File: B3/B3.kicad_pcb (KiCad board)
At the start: 4 copper layers, 100 x 100 mm, 89 parts, among them SW301 SW_SPDT, U301 74HC00, U302 74HC125, U303 74HC74, U304 74HC74, U305 74HC74, U306 74HC32, U307 74HC299, U308 74HC193, U309 74HC00, U310 74HC244, U311 74HC377, U312 74HC244, U313 74HC299, U314 74HC32, U315 74HC193, U316 74HC00, U317 74HC74, U318 74HC08, U319 74HC32, U320 74HC00, U321 74HC00, U322 74HC00, U323 74HC00, U324 74HC00, U325 74HC08, U326 74HC08, U327 74HC377, U328 74HC00, U329 74HC00, U330 74HC74, U331 74HC74, U332 74HC74, U333 74HC74, U334 74HC74, U335 74HC04, U336 74HC244, U337 74HC08, U338 74HC32, U339 74HC08, U340 74HC74

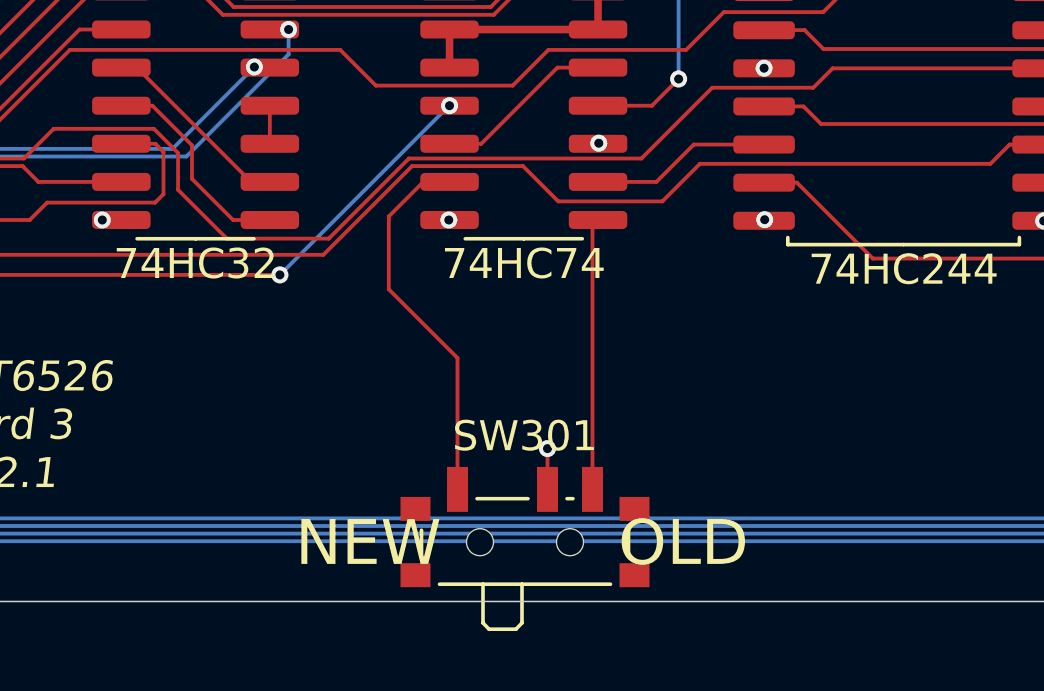
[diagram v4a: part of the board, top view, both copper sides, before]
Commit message: Issue #12 diagnosis
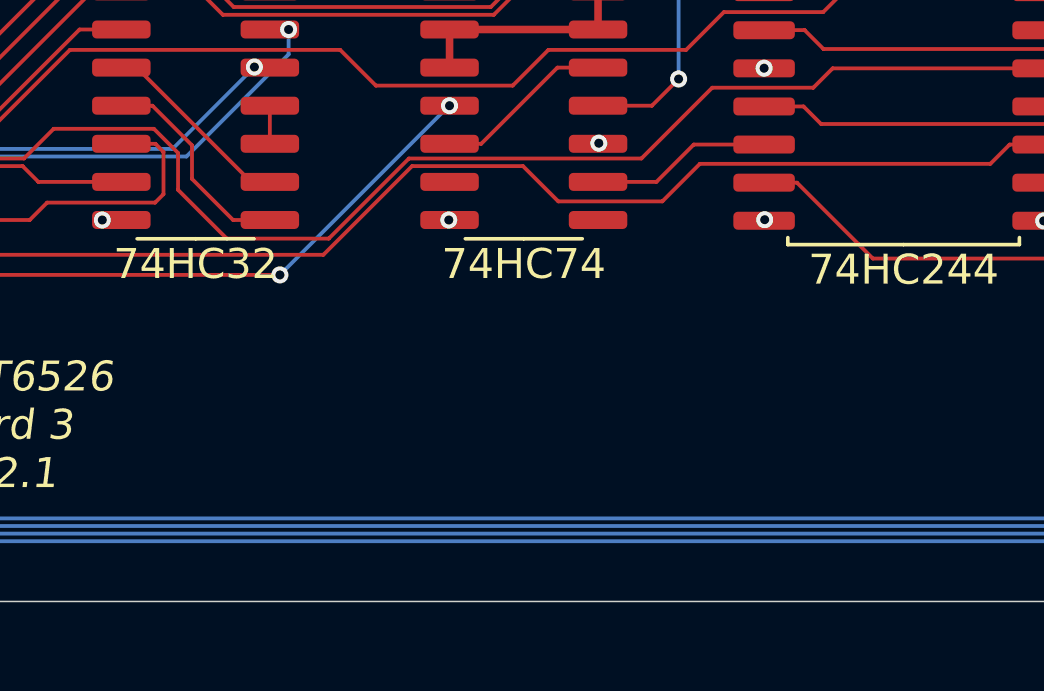
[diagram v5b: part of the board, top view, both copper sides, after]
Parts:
- removed SW301: SW_SPDT, Button_Switch_SMD:SW_SPDT_PCM12
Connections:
- U334 pad 6: Net-(U334-Pad6) -> unconnected-(U334-Pad6)
- U334 pad 8: Net-(U334-Pad8) -> ~{IRQ}
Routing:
- net ~{IRQ}: track 55.2 -> 0.00 mm, vias 1 -> 0
- net Net-(U334-Pad6): track 11.7 -> 0.00 mm
- net Net-(U334-Pad8): track 8.80 -> 0.00 mm
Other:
- board text removed: "NEW OLD"
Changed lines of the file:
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@@
   (net 155 "/icr/icrControl/ICR1")
   (net 156 "Net-(U334-Pad4)")
-  (net 157 "Net-(U334-Pad6)")
+  (net 157 "unconnected-(U334-Pad6)")
   (net 158 "/icr/icrControl/ICR7")
   (net 159 "Net-(U337-Pad8)")
@@
   (net 212 "unconnected-(U340-Pad8)")
   (net 213 "unconnected-(U340-Pad9)")
-  (net 214 "Net-(U334-Pad8)")
   (footprint "Package_SO:SO-14_3.9x8.65mm_P1.27mm" (layer "F.Cu")
     (at 111.95 128.48)
@@
     )
   )
-  (footprint "Button_Switch_SMD:SW_SPDT_PCM12" (layer "F.Cu")
-    (at 166.69 142.7)
-    (descr "Ultraminiature Surface Mount Slide Switch, right-angle, https://www.ckswitches.com/media/1424/pcm.pdf")
-    (property "Sheetfile" "icrControl.kicad_sch")
-    (property "Sheetname" "icrControl")
-    (attr smd)
-    (fp_text reference "SW301" (at 0 -3.2) (layer "F.SilkS")
-      (effects (font (size 1 1) (thickness 0.15)))
-    )
-    (fp_text value "SW_SPDT" (at 0 4.25) (layer "F.Fab")
-      (effects (font (size 1 1) (thickness 0.15)))
-    )
-    (fp_text user "${REFERENCE}" (at 0 -3.2) (layer "F.Fab")
-      (effects (font (size 1 1) (thickness 0.15)))
-    )
-    (fp_line (start 3.45 0.72) (end 3.45 -0.07) (layer "F.SilkS") (width 0.12))
-    (fp_line (start -0.1 3.02) (end -0.1 1.73) (layer "F.SilkS") (width 0.12))
-    (fp_line (start -1.2 3.23) (end -0.3 3.23) (layer "F.SilkS") (width 0.12))
-    (fp_line (start 1.4 -1.12) (end 1.6 -1.12) (layer "F.SilkS") (width 0.12))
-    (fp_line (start -0.1 3.02) (end -0.3 3.23) (layer "F.SilkS") (width 0.12))
-    (fp_line (start -1.4 3.02) (end -1.2 3.23) (layer "F.SilkS") (width 0.12))
-    (fp_line (start -3.45 -0.07) (end -3.45 0.72) (layer "F.SilkS") (width 0.12))
-    (fp_line (start -2.85 1.73) (end 2.85 1.73) (layer "F.SilkS") (width 0.12))
-    (fp_line (start -1.4 1.73) (end -1.4 3.02) (layer "F.SilkS") (width 0.12))
-    (fp_line (start -1.6 -1.12) (end 0.1 -1.12) (layer "F.SilkS") (width 0.12))
-    (fp_line (start -4.4 -2.45) (end 4.4 -2.45) (layer "F.CrtYd") (width 0.05))
-    (fp_line (start -1.65 3.4) (end -1.65 2.1) (layer "F.CrtYd") (width 0.05))
-    (fp_line (start 4.4 2.1) (end 1.65 2.1) (layer "F.CrtYd") (width 0.05))
-    (fp_line (start -1.65 2.1) (end -4.4 2.1) (layer "F.CrtYd") (width 0.05))
-    (fp_line (start 4.4 -2.45) (end 4.4 2.1) (layer "F.CrtYd") (width 0.05))
-    (fp_line (start -4.4 2.1) (end -4.4 -2.45) (layer "F.CrtYd") (width 0.05))
-    (fp_line (start 1.65 2.1) (end 1.65 3.4) (layer "F.CrtYd") (width 0.05))
-    (fp_line (start 1.65 3.4) (end -1.65 3.4) (layer "F.CrtYd") (width 0.05))
-    (fp_line (start -3.35 -1) (end -3.35 1.6) (layer "F.Fab") (width 0.1))
-    (fp_line (start -3.35 1.6) (end 3.35 1.6) (layer "F.Fab") (width 0.1))
-    (fp_line (start -1.4 1.65) (end -1.4 2.95) (layer "F.Fab") (width 0.1))
-    (fp_line (start -0.15 2.95) (end -0.1 2.9) (layer "F.Fab") (width 0.1))
-    (fp_line (start -0.35 3.15) (end -0.15 2.95) (layer "F.Fab") (width 0.1))
-    (fp_line (start -0.1 2.9) (end -0.1 1.6) (layer "F.Fab") (width 0.1))
-    (fp_line (start -1.4 2.95) (end -1.2 3.15) (layer "F.Fab") (width 0.1))
-    (fp_line (start 3.35 1.6) (end 3.35 -1) (layer "F.Fab") (width 0.1))
-    (fp_line (start 3.35 -1) (end -3.35 -1) (layer "F.Fab") (width 0.1))
-    (fp_line (start -1.2 3.15) (end -0.35 3.15) (layer "F.Fab") (width 0.1))
-    (pad "" smd rect (at 3.65 -0.78) (size 1 0.8) (layers "F.Cu" "F.Paste" "F.Mask"))
-    (pad "" smd rect (at -3.65 -0.78) (size 1 0.8) (layers "F.Cu" "F.Paste" "F.Mask"))
-    (pad "" np_thru_hole circle (at -1.5 0.33) (size 0.9 0.9) (drill 0.9) (layers *.Cu *.Mask))
-    (pad "" np_thru_hole circle (at 1.5 0.33) (size 0.9 0.9) (drill 0.9) (layers *.Cu *.Mask))
-    (pad "" smd rect (at -3.65 1.43) (size 1 0.8) (layers "F.Cu" "F.Paste" "F.Mask"))
-    (pad "" smd rect (at 3.65 1.43) (size 1 0.8) (layers "F.Cu" "F.Paste" "F.Mask"))
-    (pad "1" smd rect (at -2.25 -1.43) (size 0.7 1.5) (layers "F.Cu" "F.Paste" "F.Mask")
-      (net 157 "Net-(U334-Pad6)") (pinfunction "A") (pintype "passive"))
-    (pad "2" smd rect (at 0.75 -1.43) (size 0.7 1.5) (layers "F.Cu" "F.Paste" "F.Mask")
-      (net 19 "~{IRQ}") (pinfunction "B") (pintype "passive"))
-    (pad "3" smd rect (at 2.25 -1.43) (size 0.7 1.5) (layers "F.Cu" "F.Paste" "F.Mask")
-      (net 214 "Net-(U334-Pad8)") (pinfunction "C") (pintype "passive"))
-    (model "${KICAD6_3DMODEL_DIR}/Button_Switch_SMD.3dshapes/SW_SPDT_PCM12.wrl"
-      (offset (xyz 0 0 0))
-      (scale (xyz 1 1 1))
-      (rotate (xyz 0 0 0))
-    )
-  )
   (footprint "Connector_PinHeader_2.54mm:PinHeader_2x10_P2.54mm_Vertical" (layer "F.Cu")
     (at 192.5 132.66 180)
@@
       (net 169 "Net-(U334-Pad12)") (pinfunction "Q") (pintype "output"))
     (pad "6" smd roundrect (at -2.475 2.54) (size 1.95 0.6) (layers "F.Cu" "F.Paste" "F.Mask") (roundrect_rratio 0.25)
-      (net 157 "Net-(U334-Pad6)") (pinfunction "~{Q}") (pintype "output"))
+      (net 157 "unconnected-(U334-Pad6)") (pinfunction "~{Q}") (pintype "output+no_connect"))
     (pad "7" smd roundrect (at -2.475 3.81) (size 1.95 0.6) (layers "F.Cu" "F.Paste" "F.Mask") (roundrect_rratio 0.25)
       (net 30 "GND") (pinfunction "GND") (pintype "power_in"))
     (pad "8" smd roundrect (at 2.475 3.81) (size 1.95 0.6) (layers "F.Cu" "F.Paste" "F.Mask") (roundrect_rratio 0.25)
-      (net 214 "Net-(U334-Pad8)") (pinfunction "~{Q}") (pintype "output"))
+      (net 19 "~{IRQ}") (pinfunction "~{Q}") (pintype "output"))
     (pad "9" smd roundrect (at 2.475 2.54) (size 1.95 0.6) (layers "F.Cu" "F.Paste" "F.Mask") (roundrect_rratio 0.25)
       (net 158 "/icr/icrControl/ICR7") (pinfunction "Q") (pintype "output"))
@@
     (effects (font (size 1 1) (thickness 0.25) italic))
   )
-  (gr_text "NEW         OLD" (at 166.59 143.06) (layer "F.SilkS")
-    (effects (font (size 1.5 1.5) (thickness 0.3)))
-  )
   (via (at 108.83 84.56) (size 0.57) (drill 0.3) (layers "F.Cu" "B.Cu") (net 1))
   (segment (start 106.95 86.44) (end 106.95 141.07) (width 0.127) (layer "In2.Cu") (net 1))
@@
   (segment (start 195.64704 115.48704) (end 195.64704 134.291492) (width 0.127) (layer "B.Cu") (net 17))
   (segment (start 192.5 112.34) (end 195.64704 115.48704) (width 0.127) (layer "B.Cu") (net 17))
-  (segment (start 167.44 141.27) (end 167.44 139.91) (width 0.127) (layer "F.Cu") (net 19))
-  (via (at 167.44 139.91) (size 0.57) (drill 0.3) (layers "F.Cu" "B.Cu") (net 19))
-  (segment (start 167.44 139.91) (end 167.91 139.91) (width 0.127) (layer "In2.Cu") (net 19))
-  (segment (start 171.96 143.96) (end 180.52 143.96) (width 0.127) (layer "In2.Cu") (net 19))
-  (segment (start 167.91 139.91) (end 171.96 143.96) (width 0.127) (layer "In2.Cu") (net 19))
-  (segment (start 180.52 143.96) (end 191.21 133.27) (width 0.127) (layer "In2.Cu") (net 19))
-  (segment (start 191.21 133.27) (end 191.21 111.09) (width 0.127) (layer "In2.Cu") (net 19))
-  (segment (start 191.21 111.09) (end 192.5 109.8) (width 0.127) (layer "In2.Cu") (net 19))
   (segment (start 162.52 112.8) (end 164.145 112.8) (width 0.127) (layer "F.Cu") (net 20))
   (segment (start 167.23 103.53) (end 169.105 103.53) (width 0.127) (layer "F.Cu") (net 20))
@@
   (segment (start 164.175 128.48) (end 164.16 128.48) (width 0.127) (layer "B.Cu") (net 156))
   (segment (start 164.16 128.48) (end 158.52 134.12) (width 0.127) (layer "B.Cu") (net 156))
-  (segment (start 162.15 134.6) (end 164.44 136.89) (width 0.127) (layer "F.Cu") (net 157))
-  (segment (start 162.15 132.17) (end 162.15 134.6) (width 0.127) (layer "F.Cu") (net 157))
-  (segment (start 163.3 131.02) (end 162.15 132.17) (width 0.127) (layer "F.Cu") (net 157))
-  (segment (start 164.44 136.89) (end 164.44 141.27) (width 0.127) (layer "F.Cu") (net 157))
   (segment (start 169.125 131.02) (end 171.07 131.02) (width 0.127) (layer "F.Cu") (net 158))
   (segment (start 172.315 129.775) (end 174.66 129.775) (width 0.127) (layer "F.Cu") (net 158))
@@
   (segment (start 137.46 119.18) (end 136.305 119.18) (width 0.127) (layer "F.Cu") (net 210))
   (segment (start 131.355 111.56) (end 132.43 111.56) (width 0.127) (layer "F.Cu") (net 210))
-  (segment (start 168.94 132.475) (end 168.94 141.27) (width 0.127) (layer "F.Cu") (net 214))
   (zone (net 0) (net_name "") (layers "F.Cu" "In2.Cu" "B.Cu") (hatch edge 0.508)
     (connect_pads (clearance 0))

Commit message: Ready for v0.2.2
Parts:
- added C341: 100n, Capacitor_SMD:C_0603_1608Metric, F.Cu at (182.6, 130.3)
- added C342: 100n, Capacitor_SMD:C_0603_1608Metric, F.Cu at (170.4, 134.8)
- added SW301: SW_SPDT, Button_Switch_SMD:SW_SPDT_PCM12, F.Cu at (188.1, 142.8)
- added U341: 74HC157, Package_SO:SO-16_3.9x9.9mm_P1.27mm, F.Cu at (178.8, 136.3)
- added U342: 74HC74, Package_SO:SO-14_3.9x8.65mm_P1.27mm, F.Cu at (166.6, 140.2)
- U302: value 74HC125 -> 74HCT125
- U305: value 74HC74 -> 74HCT74
- U335: value 74HC04 -> 74HCT04
- moved C328 4.91 mm to (184.7, 114.1)
- moved U336 4.89 mm to (179.3, 121.7)
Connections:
- U330 pad 6: /icr/icrControl/~{ICRCLR} -> /icr/icrControl/~{ICRCLR2}
- U330 pad 8: unconnected-(U330-Pad8) -> /icr/icrControl/~{ICRCLR1}
- U331 pad 1: /icr/icrControl/~{ICRCLR} -> /icr/icrControl/~{ICRCLR1}
- U331 pad 13: /icr/icrControl/~{ICRCLR} -> /icr/icrControl/~{ICRCLR1}
- U332 pad 1: /icr/icrControl/~{ICRCLR} -> /icr/icrControl/~{ICRCLR1}
- U332 pad 13: /icr/icrControl/~{ICRCLR} -> Net-(U332-Pad13)
- U333 pad 13: /icr/icrControl/~{ICRCLR} -> /icr/icrControl/~{ICRCLR1}
- U334 pad 1: /icr/icrControl/~{ICRCLR} -> /icr/icrControl/~{ICRCLR1}
- U334 pad 13: VCC -> /icr/icrControl/~{ICRCLR1}
- U334 pad 8: ~{IRQ} -> unconnected-(U334-Pad8)
- U334 pad 9: /icr/icrControl/ICR7 -> Net-(U334-Pad9)
- U337 pad 12: /icr/icrControl/ICR1 -> TBPULSE
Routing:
- net /icr/icrControl/~{ICRCLR1}: track 0.00 -> 105.5 mm, vias 0 -> 5
- net Net-(U332-Pad13): track 0.00 -> 85.2 mm, vias 0 -> 2
- net /icr/icrControl/~{ICRCLR}: track 68.2 -> 0.00 mm, vias 2 -> 0
- net /icr/icrControl/~{ICRCLR2}: track 0.00 -> 48.8 mm, vias 0 -> 2
- net ~{IRQ}: track 0.00 -> 43.8 mm, vias 0 -> 1
- net TBPULSE: track 131.3 -> 158.4 mm, vias 1 -> 2
- net Net-(SW301-Pad2): track 0.00 -> 18.4 mm
- net Net-(U341-Pad11): track 0.00 -> 18.3 mm
- net Net-(U334-Pad12): track 6.00 -> 24.0 mm, vias 0 -> 2
- net Net-(U334-Pad9): track 0.00 -> 16.7 mm
- net /~{PHI2}: track 198.7 -> 214.8 mm, vias 10 -> 11
- net /icr/icrControl/ICR7: track 6.05 -> 21.0 mm
- net Net-(U341-Pad10): track 0.00 -> 14.1 mm
- net GND: track 75.6 -> 85.0 mm, vias 92 -> 97
- net Net-(U334-Pad4): track 52.1 -> 61.3 mm
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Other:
- board text added: "74HCT6526 Board 3 v0.2.2"
- board text added: "NEW OLD"
- board text removed: "74HCT6526 Board 3 v0.2.1"
